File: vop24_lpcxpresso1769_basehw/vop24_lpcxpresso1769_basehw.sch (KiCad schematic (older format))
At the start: 2 parts

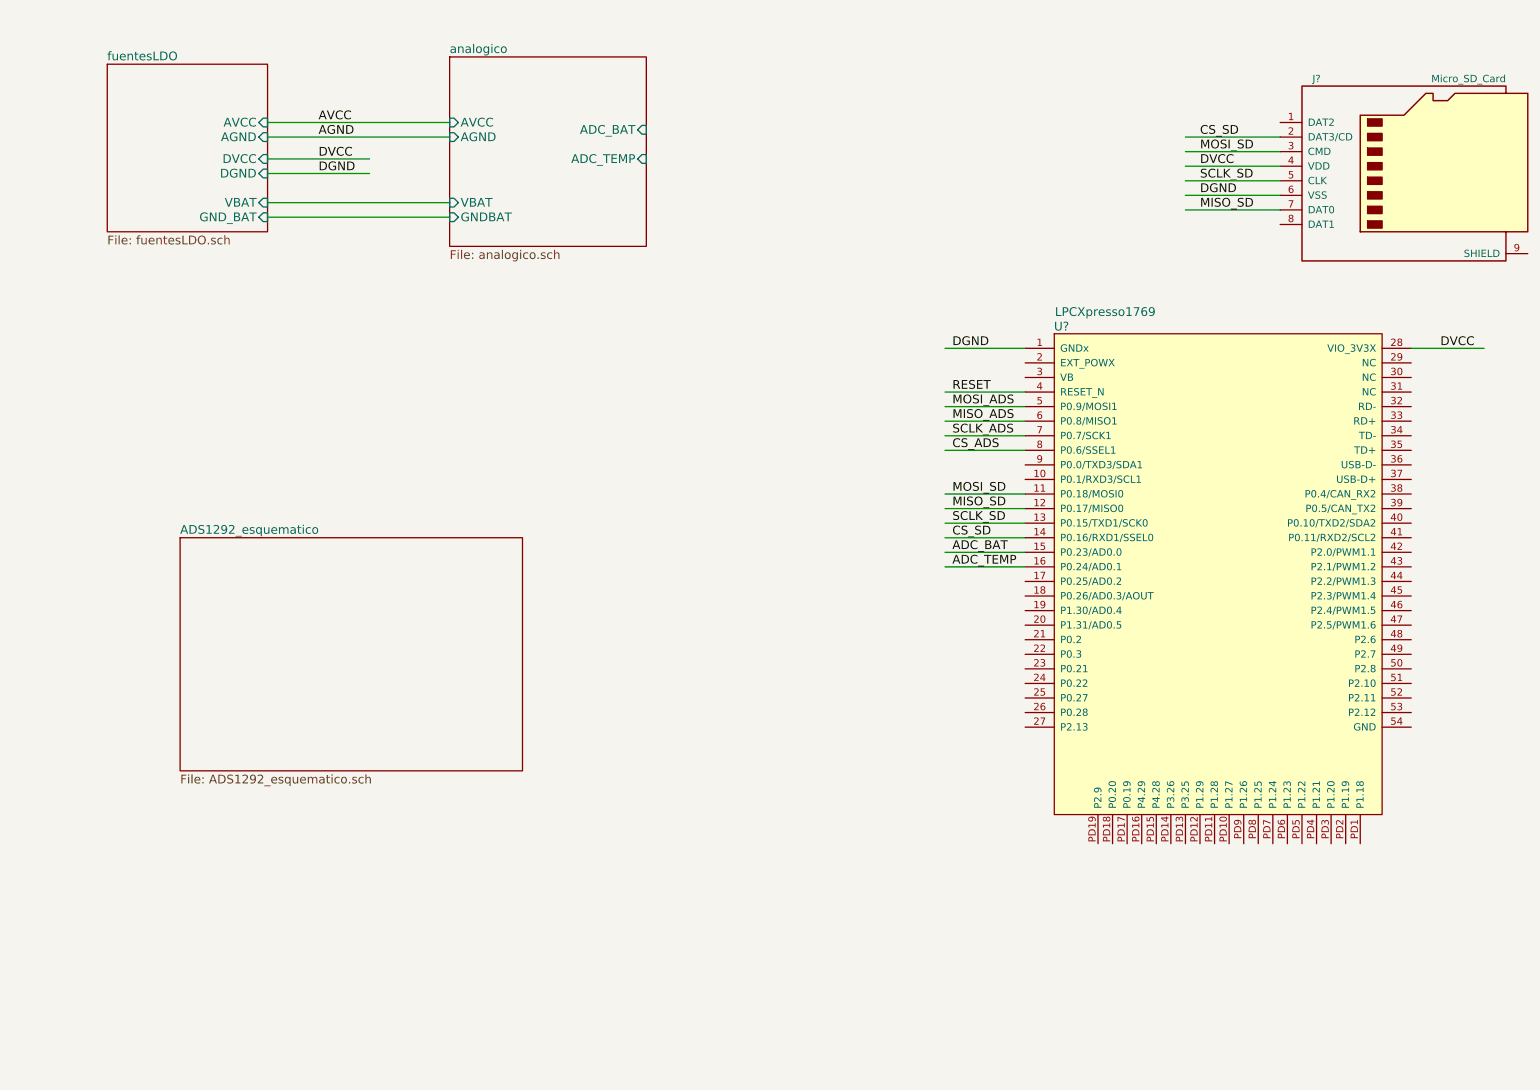
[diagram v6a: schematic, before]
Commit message: Esquematico ADS:    - version a revisar. Falta agregar medicion de bateria y carga USB como en la nota de aplicacion
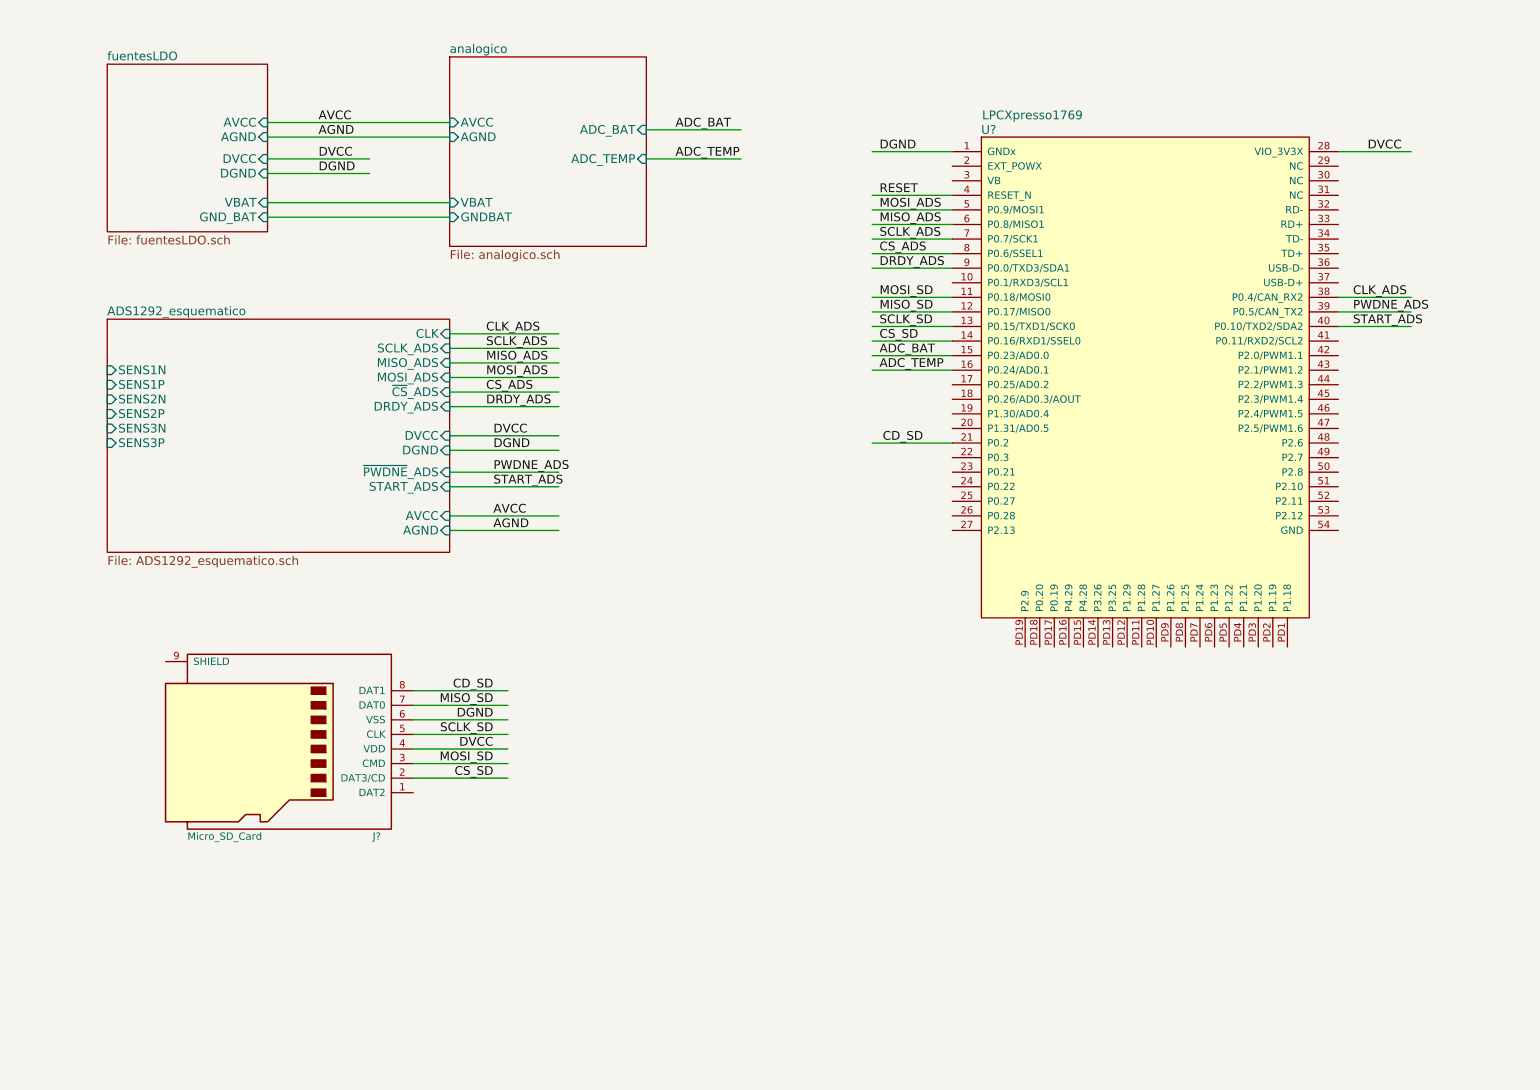
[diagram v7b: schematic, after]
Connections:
- net labels added: CD_SD, CLK_ADS, DRDY_ADS, PWDNE_ADS, START_ADS
- wire segments 25 -> 45
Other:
- moved on the sheet: J?, U?
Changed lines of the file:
@@
 L Micro_SD_Card J?
 U 1 1 5B33BAF7
-P 10150 1550
-F 0 "J?" H 9500 2150 50  0000 C CNN
-F 1 "Micro_SD_Card" H 10800 2150 50  0000 R CNN
-F 2 "" H 11300 1850 50  0001 C CNN
-F 3 "" H 10150 1550 50  0001 C CNN
-	1    10150 1550
-	1    0    0    -1
+P 2400 5550
+F 0 "J?" H 1750 6150 50  0000 C CNN
+F 1 "Micro_SD_Card" H 3050 6150 50  0000 R CNN
+F 2 "" H 3550 5850 50  0001 C CNN
+F 3 "" H 2400 5550 50  0001 C CNN
+	1    2400 5550
+	-1   0    0    1
 $EndComp
-Text Label 8700 1350 0    60   ~ 0
+Text Label 3850 5750 2    60   ~ 0
 CS_SD
-Text Label 8700 1650 0    60   ~ 0
+Text Label 3850 5450 2    60   ~ 0
 SCLK_SD
-Text Label 8700 1450 0    60   ~ 0
+Text Label 3850 5650 2    60   ~ 0
 MOSI_SD
-Text Label 8700 1550 0    60   ~ 0
-DVCC
-Text Label 8700 1750 0    60   ~ 0
-DGND
-Text Label 8700 1850 0    60   ~ 0
+Text Label 3850 5550 2    60   ~ 0
+DVCC
+Text Label 3850 5350 2    60   ~ 0
+DGND
+Text Label 3850 5250 2    60   ~ 0
 MISO_SD
 $Comp
 L LPCXpresso1769 U?
 U 1 1 5B343F3C
-P 8850 4350
-F 0 "U?" H 7750 6050 60  0000 C CNN
-F 1 "LPCXpresso1769" H 8050 6150 60  0000 C CNN
-F 2 "" H 8550 4750 60  0001 C CNN
-F 3 "" H 8550 4750 60  0001 C CNN
-	1    8850 4350
+P 8350 3000
+F 0 "U?" H 7250 4700 60  0000 C CNN
+F 1 "LPCXpresso1769" H 7550 4800 60  0000 C CNN
+F 2 "" H 8050 3400 60  0001 C CNN
+F 3 "" H 8050 3400 60  0001 C CNN
+	1    8350 3000
 	1    0    0    -1
 $EndComp
-Text Label 7000 2800 0    60   ~ 0
-DGND
-Text Label 7000 4200 0    60   ~ 0
+Text Label 6500 1450 0    60   ~ 0
+DGND
+Text Label 6500 2850 0    60   ~ 0
 ADC_BAT
-Text Label 7000 4300 0    60   ~ 0
+Text Label 6500 2950 0    60   ~ 0
 ADC_TEMP
-Text Label 10350 2800 0    60   ~ 0
-DVCC
-Text Label 7000 3100 0    60   ~ 0
+Text Label 9850 1450 0    60   ~ 0
+DVCC
+Text Label 6500 1750 0    60   ~ 0
 RESET
-Text Label 7000 3800 0    60   ~ 0
+Text Label 6500 2450 0    60   ~ 0
 MOSI_SD
-Text Label 7000 3900 0    60   ~ 0
+Text Label 6500 2550 0    60   ~ 0
 MISO_SD
-Text Label 7000 4000 0    60   ~ 0
+Text Label 6500 2650 0    60   ~ 0
 SCLK_SD
-Text Label 7000 4100 0    60   ~ 0
+Text Label 6500 2750 0    60   ~ 0
 CS_SD
-Text Label 7000 3500 0    60   ~ 0
+Text Label 6500 2150 0    60   ~ 0
 CS_ADS
-Text Label 7000 3200 0    60   ~ 0
+Text Label 6500 1850 0    60   ~ 0
 MOSI_ADS
-Text Label 7000 3400 0    60   ~ 0
+Text Label 6500 2050 0    60   ~ 0
 SCLK_ADS
-Text Label 7000 3300 0    60   ~ 0
+Text Label 6500 1950 0    60   ~ 0
 MISO_ADS
-Wire Wire Line
-	9250 1350 8600 1350
-Wire Wire Line
-	9250 1450 8600 1450
-Wire Wire Line
-	9250 1550 8600 1550
-Wire Wire Line
-	9250 1650 8600 1650
-Wire Wire Line
-	9250 1750 8600 1750
-Wire Wire Line
-	9250 1850 8600 1850
-Wire Wire Line
-	7500 2800 6950 2800
-Wire Wire Line
-	7500 4200 6950 4200
-Wire Wire Line
-	7500 4300 6950 4300
-Wire Wire Line
-	10150 2800 10650 2800
-Wire Wire Line
-	7500 3100 6950 3100
-Wire Wire Line
-	7500 3800 6950 3800
-Wire Wire Line
-	6950 3900 7500 3900
-Wire Wire Line
-	7500 4000 6950 4000
-Wire Wire Line
-	7500 4100 6950 4100
-Wire Wire Line
-	7500 3200 6950 3200
-Wire Wire Line
-	6950 3300 7500 3300
-Wire Wire Line
-	7500 3400 6950 3400
-Wire Wire Line
-	6950 3500 7500 3500
 $Sheet
 S 1200 850  1100 1150
@@
 F7 "GND_BAT" I R 2300 1900 60
 $EndSheet
-Wire Wire Line
-	2300 1250 3550 1250
-Wire Wire Line
-	2300 1350 3550 1350
-Wire Wire Line
-	2300 1500 3000 1500
-Wire Wire Line
-	2300 1600 3000 1600
 Text Label 2650 1350 0    60   ~ 0
 AGND
@@
 F7 "GNDBAT" I L 3550 1900 60
 $EndSheet
-Wire Wire Line
-	2300 1800 3550 1800
-Wire Wire Line
-	3550 1900 2300 1900
 $Sheet
-S 1700 4100 2350 1600
+S 1200 2600 2350 1600
 U 5B3D4A05
 F0 "ADS1292_esquematico" 60
 F1 "ADS1292_esquematico.sch" 60
+F2 "AVCC" I R 3550 3950 60
+F3 "AGND" I R 3550 4050 60
+F4 "DVCC" I R 3550 3400 60
+F5 "DGND" I R 3550 3500 60
+F6 "DRDY_ADS" I R 3550 3200 60
+F7 "MISO_ADS" I R 3550 2900 60
+F8 "SCLK_ADS" I R 3550 2800 60
+F9 "MOSI_ADS" I R 3550 3000 60
+F10 "~CS~_ADS" I R 3550 3100 60
+F11 "~PWDNE~_ADS" I R 3550 3650 60
+F12 "START_ADS" I R 3550 3750 60
+F13 "CLK" I R 3550 2700 60
+F14 "SENS1N" I L 1200 2950 60
+F15 "SENS1P" I L 1200 3050 60
+F16 "SENS2N" I L 1200 3150 60
+F17 "SENS2P" I L 1200 3250 60
+F18 "SENS3N" I L 1200 3350 60
+F19 "SENS3P" I L 1200 3450 60
 $EndSheet
+Text Label 3800 3000 0    60   ~ 0
+MOSI_ADS
+Text Label 3800 2900 0    60   ~ 0
+MISO_ADS
+Text Label 3800 3100 0    60   ~ 0
+CS_ADS
+Text Label 3800 2800 0    60   ~ 0
+SCLK_ADS
+Text Label 3850 3400 0    60   ~ 0
+DVCC
+Text Label 3850 3500 0    60   ~ 0
+DGND
+Text Label 3850 3950 0    60   ~ 0
+AVCC
+Text Label 3850 4050 0    60   ~ 0
+AGND
+Text Label 3800 3200 0    60   ~ 0
+DRDY_ADS
+Text Label 6500 2250 0    60   ~ 0
+DRDY_ADS
+Text Label 3850 3650 0    60   ~ 0
+PWDNE_ADS
+Text Label 3850 3750 0    60   ~ 0
+START_ADS
+Text Label 3800 2700 0    60   ~ 0
+CLK_ADS
+Text Label 9750 2650 0    60   ~ 0
+START_ADS
+Text Label 9750 2550 0    60   ~ 0
+PWDNE_ADS
+Text Label 9750 2450 0    60   ~ 0
+CLK_ADS
+Text Label 3850 5150 2    60   ~ 0
+CD_SD
+Wire Wire Line
+	3300 5750 3950 5750
+Wire Wire Line
+	3300 5650 3950 5650
+Wire Wire Line
+	3300 5550 3950 5550
+Wire Wire Line
+	3300 5450 3950 5450
+Wire Wire Line
+	3300 5350 3950 5350
+Wire Wire Line
+	3300 5250 3950 5250
+Wire Wire Line
+	7000 1450 6450 1450
+Wire Wire Line
+	7000 2850 6450 2850
+Wire Wire Line
+	7000 2950 6450 2950
+Wire Wire Line
+	9650 1450 10150 1450
+Wire Wire Line
+	7000 1750 6450 1750
+Wire Wire Line
+	7000 2450 6450 2450
+Wire Wire Line
+	6450 2550 7000 2550
+Wire Wire Line
+	7000 2650 6450 2650
+Wire Wire Line
+	7000 2750 6450 2750
+Wire Wire Line
+	7000 1850 6450 1850
+Wire Wire Line
+	6450 1950 7000 1950
+Wire Wire Line
+	7000 2050 6450 2050
+Wire Wire Line
+	6450 2150 7000 2150
+Wire Wire Line
+	2300 1250 3550 1250
+Wire Wire Line
+	2300 1350 3550 1350
+Wire Wire Line
+	2300 1500 3000 1500
+Wire Wire Line
+	2300 1600 3000 1600
+Wire Wire Line
+	2300 1800 3550 1800
+Wire Wire Line
+	3550 1900 2300 1900
+Wire Wire Line
+	3550 2800 4300 2800
+Wire Wire Line
+	3550 2900 4300 2900
+Wire Wire Line
+	3550 3000 4300 3000
+Wire Wire Line
+	3550 3100 4300 3100
+Wire Wire Line
+	3550 3200 4300 3200
+Wire Wire Line
+	3550 3400 4300 3400
+Wire Wire Line
+	3550 3500 4300 3500
+Wire Wire Line
+	3550 3950 4300 3950
+Wire Wire Line
+	3550 4050 4300 4050
+Wire Wire Line
+	3550 2700 4300 2700
+Wire Wire Line
+	3550 3650 4300 3650
+Wire Wire Line
+	3550 3750 4300 3750
+Wire Wire Line
+	7000 2250 6450 2250
+Wire Wire Line
+	9650 2450 10150 2450
+Wire Wire Line
+	9650 2550 10150 2550
+Wire Wire Line
+	9650 2650 10150 2650
+Wire Wire Line
+	3300 5150 3950 5150
+Wire Wire Line
+	7000 3450 6450 3450
+Text Label 6800 3450 2    60   ~ 0
+CD_SD
+Wire Wire Line
+	4900 1300 5550 1300
+Wire Wire Line
+	4900 1500 5550 1500
+Text Label 5100 1300 0    60   ~ 0
+ADC_BAT
+Text Label 5100 1500 0    60   ~ 0
+ADC_TEMP
 $EndSCHEMATC

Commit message: Esquematico Comunicacion: falta agregar USB, BLE y UART
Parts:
- J?: symbol Micro_SD_Card -> vop24_lpcxpresso1769_basehw-rescue:Micro_SD_Card
- U?: symbol LPCXpresso1769 -> vop24_lpcxpresso1769_basehw-rescue:LPCXpresso1769
